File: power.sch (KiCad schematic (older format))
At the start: 51 parts, among them J2 PJ-002B, J4 Screw_Terminal_01x12, U11 LT3471, U14 LP38693MP-5.0, U15 ADP150AUJZ-3.3-R7, U17 LM2937xMP, U19 MAX6070BAUT21+T, U20 LP5907MFX-1.8, U21 MC79M15_TO252

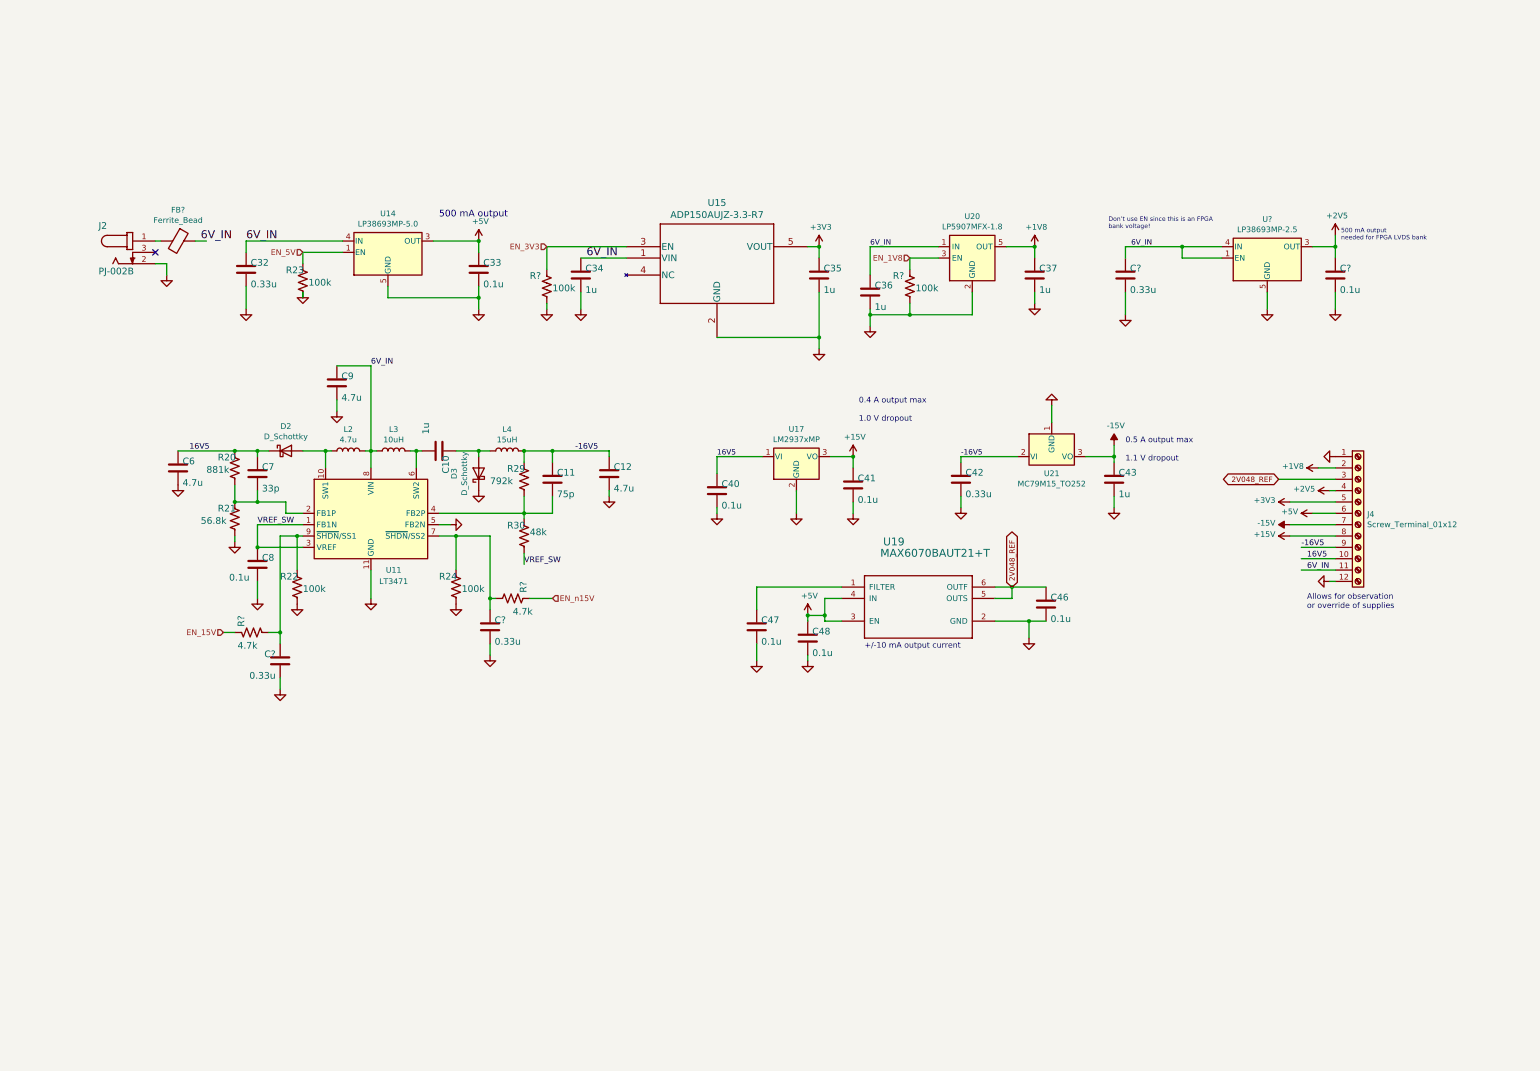
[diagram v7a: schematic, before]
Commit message: modifications to power page for EN jumpers. Switched to all TI linear reg.
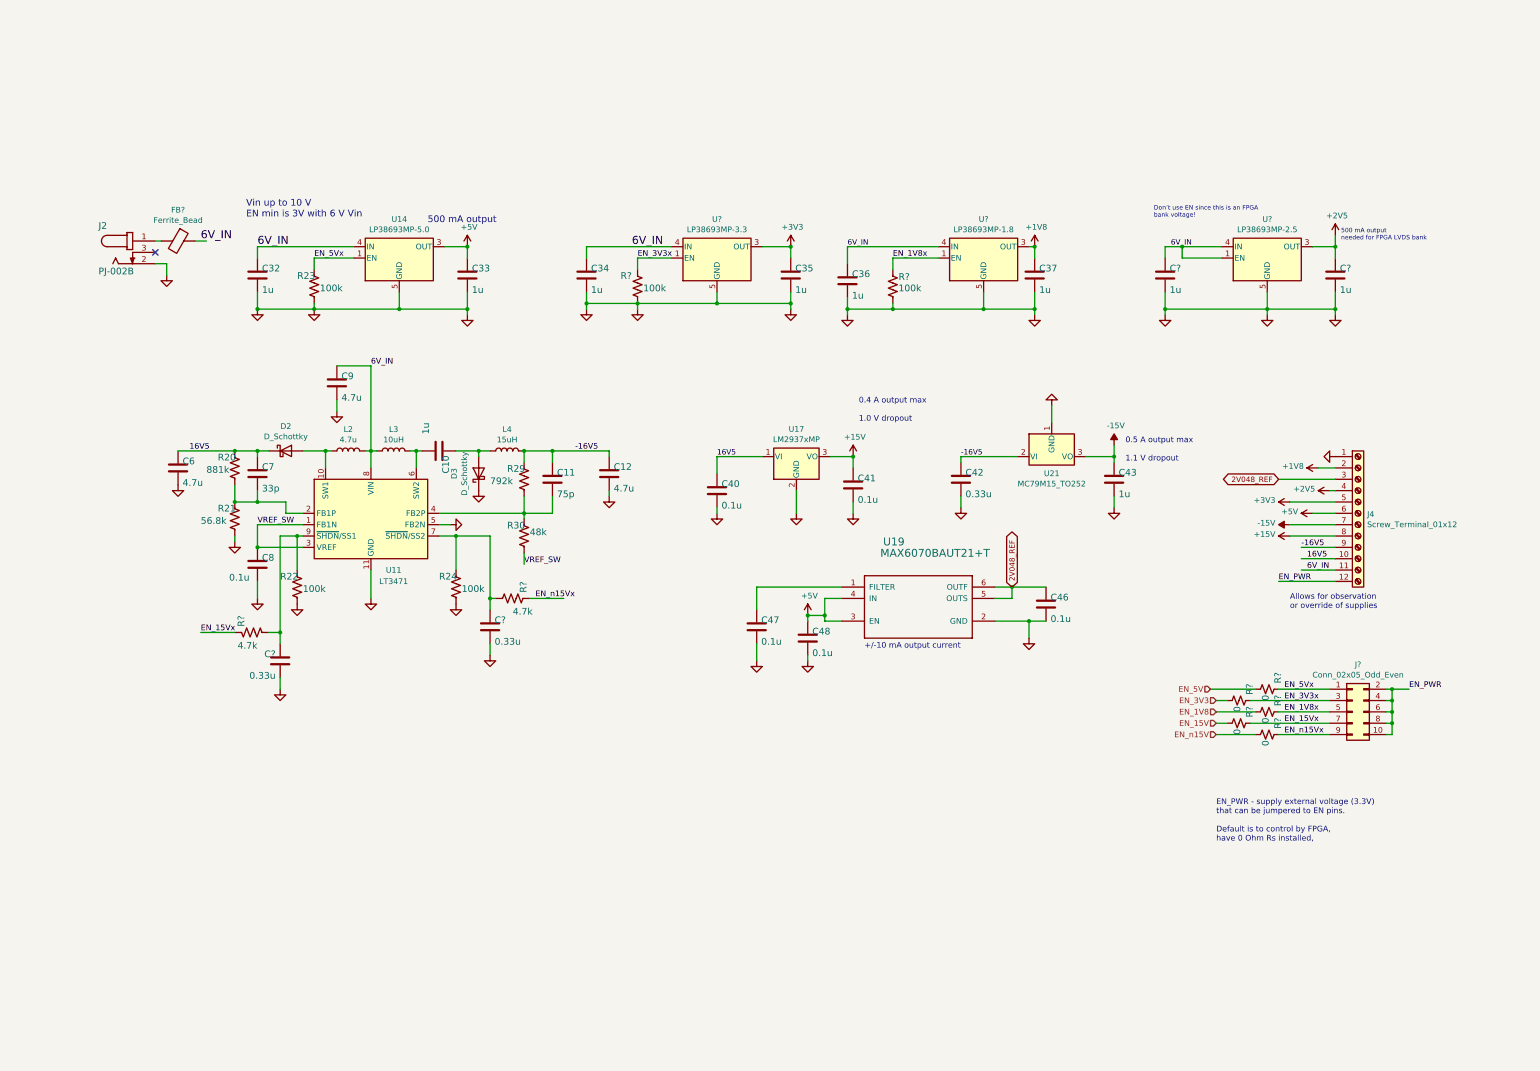
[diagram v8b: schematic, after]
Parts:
- removed U15: ADP150AUJZ-3.3-R7, adc_dac_v1:UJ_5_ADI, symbol covg-kicad:ADP150AUJZ-3.3-R7
- removed U20: LP5907MFX-1.8, Package_TO_SOT_SMD:SOT-23-5, symbol Regulator_Linear:LP5907MFX-1.8
- added J?: Conn_02x05_Odd_Even, symbol Connector_Generic:Conn_02x05_Odd_Even
- added R? (x5): 0, Resistor_SMD:R_0603_1608Metric, symbol Device:R_Small_US
- added U?: LP38693MP-1.8, Package_TO_SOT_SMD:SOT-223-5, symbol Regulator_Linear:LP38693MP-1.8
- added U?: LP38693MP-3.3, Package_TO_SOT_SMD:SOT-223-5, symbol Regulator_Linear:LP38693MP-3.3
- C32, C?: value 0.33u -> 1u
- C33, C?: value 0.1u -> 1u
- U14: Manf# (none) -> LP38693MP-5.0/NOPB
- U?: Manf# (none) -> LP38693MP-2.5/NOPB
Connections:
- net +1V8: now also U?.3 (OUT)
- net +3V3: now also U?.3 (OUT)
- net 6V_IN: now also U?.4 (IN), U?.4 (IN)
- net EN_15V: now also R?.2; no longer R?.1
- net EN_1V8: now also R?.2; no longer R?.1
- net EN_3V3: now also R?.2; no longer R?.1
- net EN_5V: now also R?.2; no longer R23.1, U14.1 (EN)
- net EN_n15V: now also R?.2; no longer R?.1
- net GND: now also U?.5 (GND), U?.5 (GND); no longer J4.12 (Pin_12)
- new net EN_15Vx: J?.7 (Pin_7), R?.1, R?.1
- new net EN_1V8x: J?.5 (Pin_5), R?.1, R?.1, U?.1 (EN)
- new net EN_3V3x: J?.3 (Pin_3), R?.1, R?.1, U?.1 (EN)
- new net EN_5Vx: J?.1 (Pin_1), R23.1, R?.1, U14.1 (EN)
- new net EN_PWR: J4.12 (Pin_12), J?.10 (Pin_10), J?.2 (Pin_2), J?.4 (Pin_4), J?.6 (Pin_6), J?.8 (Pin_8)
- new net EN_n15Vx: J?.9 (Pin_9), R?.1, R?.1
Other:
- note added: "Allows for observation \nor override of supplies"
- note added: "EN_PWR - supply external voltage (3.3V)\nthat can be jumpered to EN pins.\n\nDefault is to control by FPGA, \nhave 0 Ohm Rs installed,\n and no jumpers on the header.\n\nAlternative option is to add jumpers \n(and if EN_PWR is > 3.3 V) remove 0 Ohm."
- note added: "Vin up to 10 V\nEN min is 3V with 6 V Vin"
- note removed: "Allows for observation \nor override of supplies\n"
- moved on the sheet: C32, C33, C34, C35, C36, C?, R23, R?, U14
